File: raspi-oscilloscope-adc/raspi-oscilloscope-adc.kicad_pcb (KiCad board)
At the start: 2 copper layers, 80 x 50 mm, 25 parts, among them J1 Conn_Coaxial, J2 Conn_01x10_Male, J3 Conn_01x02_Male, SW1 SR10010F-0106-20F0B-C7-N-0027, U1 ECS-220B-100, U2 TLC5510INSR, U3 OPA690

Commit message: Tidy up
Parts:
- moved C1 74.3 mm to (127.0, 87.6)
- moved C2 74.3 mm to (167.6, 97.8)
- moved C3 74.3 mm to (180.3, 77.5)
- moved C4 74.3 mm to (157.5, 85.1)
- moved C5 74.3 mm to (170.2, 108.0)
- moved C6 74.3 mm to (170.2, 77.5)
- moved C7 74.3 mm to (154.9, 80.0)
- moved D1 74.3 mm to (157.5, 102.9)
- moved D2 74.3 mm to (121.9, 97.8)
- moved J1 74.3 mm to (119.4, 87.6)
- moved J2 74.3 mm to (182.9, 113.0)
- moved J3 74.3 mm to (139.7, 85.1)
- moved R1 74.3 mm to (129.5, 110.5)
- moved R2 74.3 mm to (157.5, 97.8)
- moved R3 74.3 mm to (152.4, 90.2)
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
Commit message: Realign pcb to grid
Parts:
- moved C2 1.27 mm to (167.6, 96.5)
- moved C4 1.27 mm to (157.5, 83.8)
- moved C7 1.27 mm to (154.9, 78.7)
- moved D1 1.27 mm to (157.5, 101.6)
- moved D2 1.27 mm to (121.9, 96.5)
- moved J3 1.27 mm to (139.7, 83.8)
- moved R2 1.27 mm to (157.5, 96.5)
- moved R5 1.27 mm to (127.0, 96.5)
- moved R6 1.27 mm to (132.1, 101.6)
- moved R7 1.27 mm to (154.9, 101.6)
- moved U1 1.27 mm to (167.6, 73.7)
- moved U3 1.27 mm to (137.2, 96.5)
- moved C1 1.27 mm to (127.0, 86.4)
- moved C3 1.27 mm to (180.3, 76.2)
- moved C5 1.27 mm to (170.2, 106.7)
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
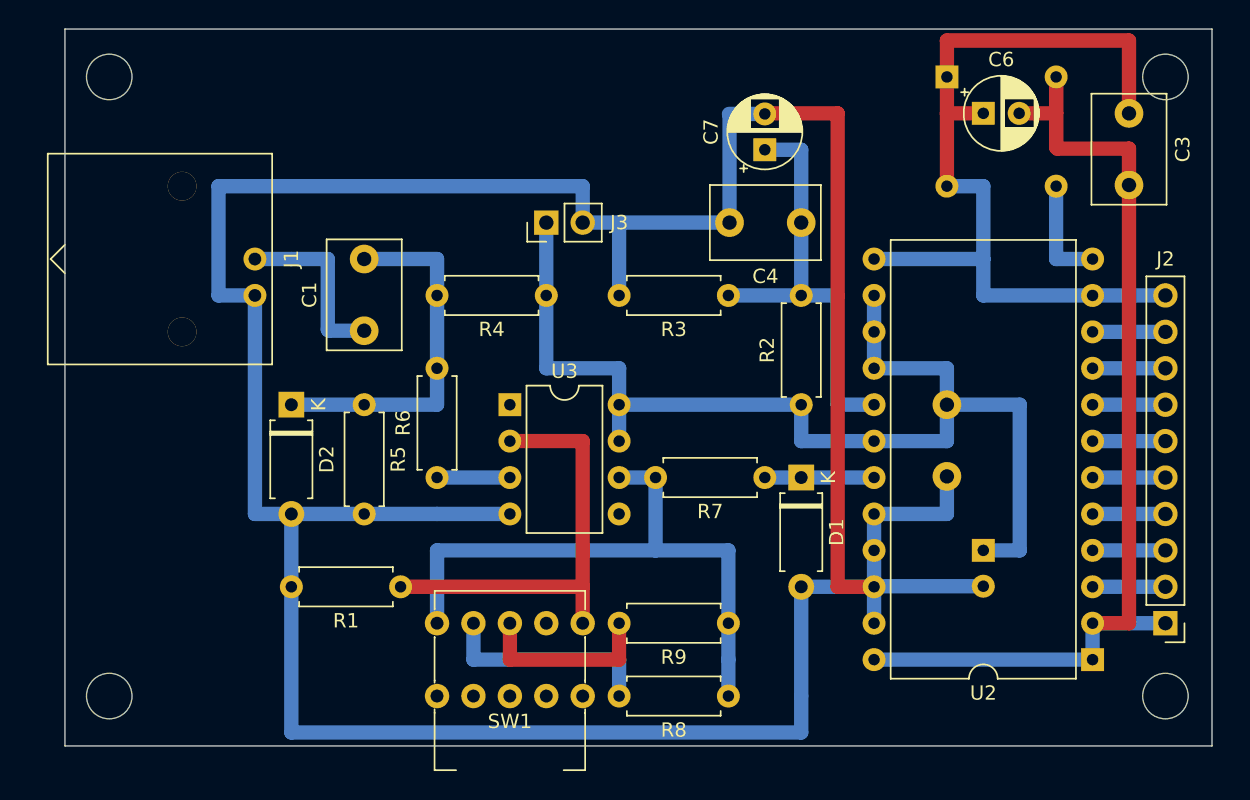
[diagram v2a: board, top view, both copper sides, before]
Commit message: Add 5V to 3V3 logic converter
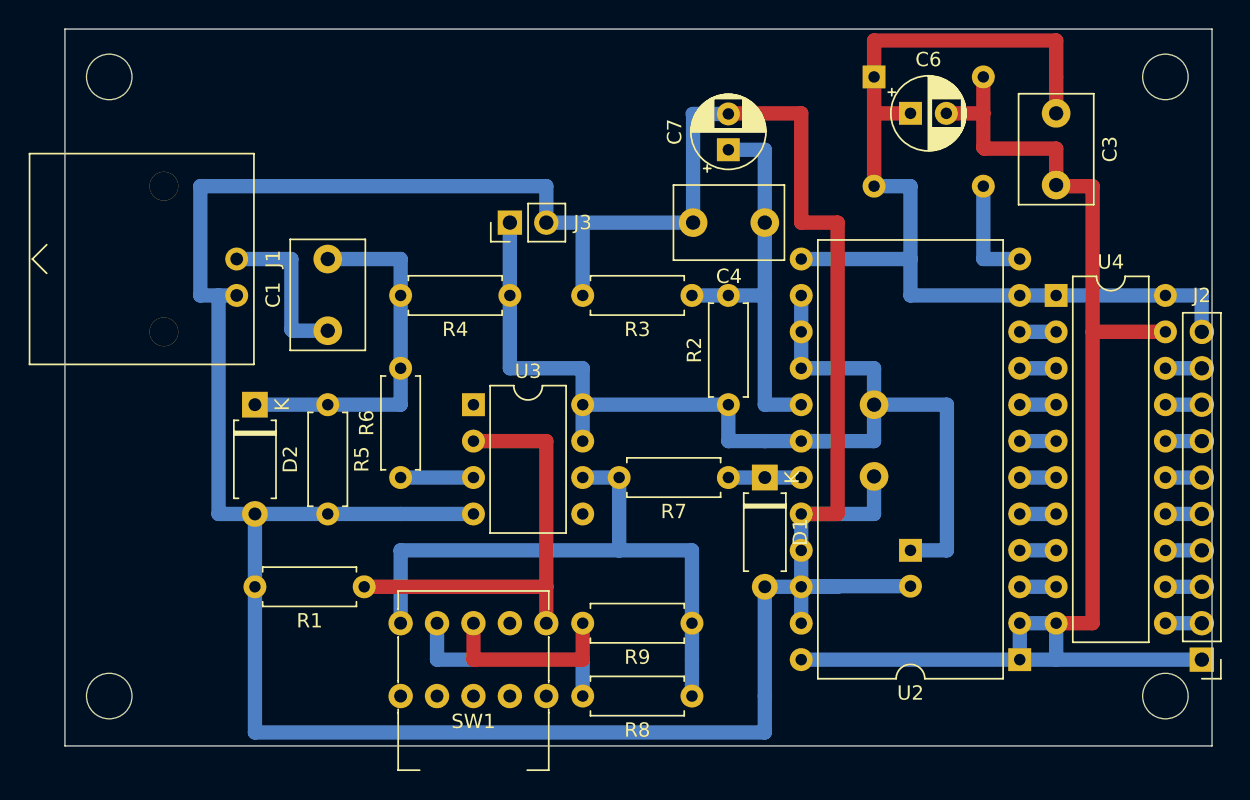
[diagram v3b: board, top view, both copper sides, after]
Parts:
- added U4: SN74LS245N, Package_DIP:DIP-20_W7.62mm, F.Cu at (175.3, 88.9)
- moved C3 5.08 mm to (175.3, 76.2)
- moved C5 5.08 mm to (165.1, 106.7)
- moved C6 5.08 mm to (165.1, 76.2)
- moved U2 5.08 mm to (172.7, 114.3)
- moved C2 5.08 mm to (162.6, 96.5)
- moved R2 5.08 mm to (152.4, 96.5)
- moved U1 5.08 mm to (162.6, 73.7)
- moved J2 3.59 mm to (185.4, 114.3)
- moved R6 2.54 mm to (129.5, 101.6)
- moved C1 2.54 mm to (124.5, 86.4)
- moved D2 2.54 mm to (119.4, 96.5)
- moved R5 2.54 mm to (124.5, 96.5)
- moved C4 2.54 mm to (154.9, 83.8)
- moved C7 2.54 mm to (152.4, 78.7)
- moved D1 2.54 mm to (154.9, 101.6)
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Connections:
- U2 pad 10: Net-(J2-Pad9) -> Net-(U2-Pad10)
- U2 pad 3: Net-(J2-Pad2) -> Net-(U2-Pad3)
- U2 pad 4: Net-(J2-Pad3) -> Net-(U2-Pad4)
- U2 pad 5: Net-(J2-Pad4) -> Net-(U2-Pad5)
- U2 pad 6: Net-(J2-Pad5) -> Net-(U2-Pad6)
- U2 pad 7: Net-(J2-Pad6) -> Net-(U2-Pad7)
- U2 pad 8: Net-(J2-Pad7) -> Net-(U2-Pad8)
- U2 pad 9: Net-(J2-Pad8) -> Net-(U2-Pad9)
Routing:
- net GNDD: track 71.1 -> 91.4 mm
- net +5VD: track 61.0 -> 71.1 mm
- net GNDA: track 226.1 -> 222.3 mm
- net Net-(J2-Pad9): track 5.08 -> 2.52 mm
- net Net-(J2-Pad8): track 5.08 -> 2.52 mm
- net Net-(J2-Pad7): track 5.08 -> 2.52 mm
- net Net-(J2-Pad6): track 5.08 -> 2.52 mm
- net Net-(J2-Pad5): track 5.08 -> 2.52 mm
- net Net-(J2-Pad4): track 5.08 -> 2.52 mm
- net Net-(J2-Pad3): track 5.08 -> 2.52 mm
- net Net-(J2-Pad2): track 5.08 -> 2.52 mm
- net Net-(D1-Pad1): track 7.62 -> 5.08 mm
- net Net-(C4-Pad1): track 30.5 -> 27.9 mm
- net Net-(U2-Pad9): track 0.00 -> 2.54 mm
- net Net-(U2-Pad8): track 0.00 -> 2.54 mm
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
